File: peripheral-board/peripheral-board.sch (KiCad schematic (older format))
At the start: 1 part

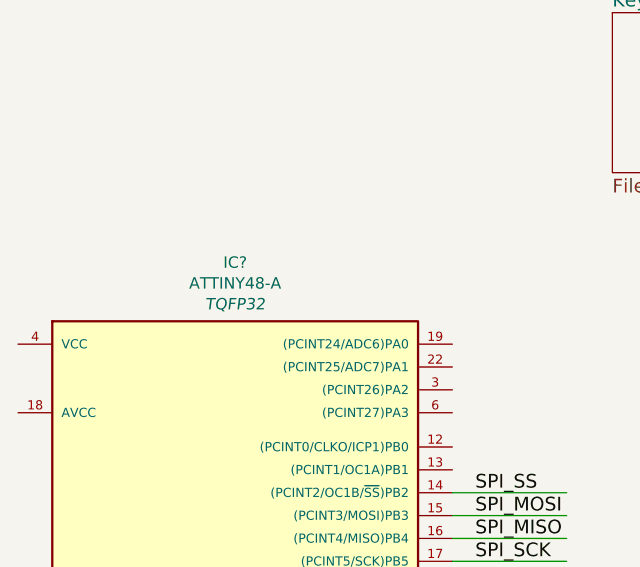
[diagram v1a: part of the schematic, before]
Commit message: added button 3d model
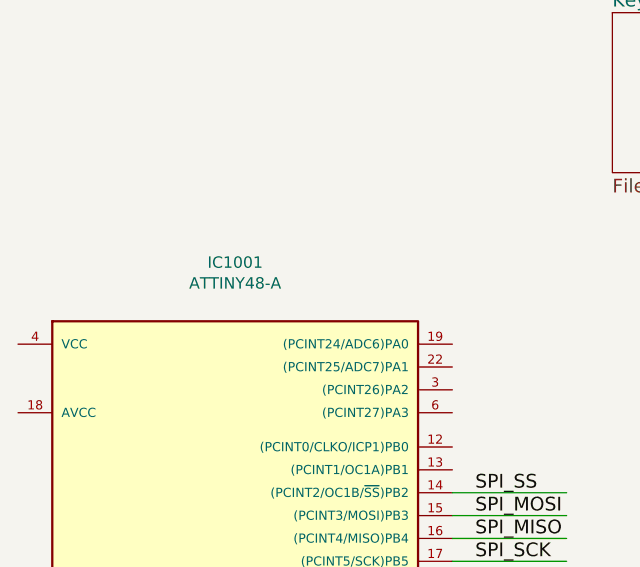
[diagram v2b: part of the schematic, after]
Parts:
- IC1001: renamed from IC?; footprint TQFP32 -> Housings_QFP:TQFP-32_7x7mm_Pitch0.8mm
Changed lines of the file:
@@
 $EndSheet
 $Comp
-L ATTINY48-A IC?
+L ATTINY48-A IC1001
 U 1 1 5819EBDE
 P 2950 4200
-F 0 "IC?" H 2950 5957 50  0000 C CNN
+F 0 "IC1001" H 2950 5957 50  0000 C CNN
 F 1 "ATTINY48-A" H 2950 5866 50  0000 C CNN
-F 2 "TQFP32" H 2950 5775 50  0000 C CIN
+F 2 "Housings_QFP:TQFP-32_7x7mm_Pitch0.8mm" H 2950 5775 50  0001 C CIN
 F 3 "" H 2950 4200 50  0000 C CNN
 	1    2950 4200

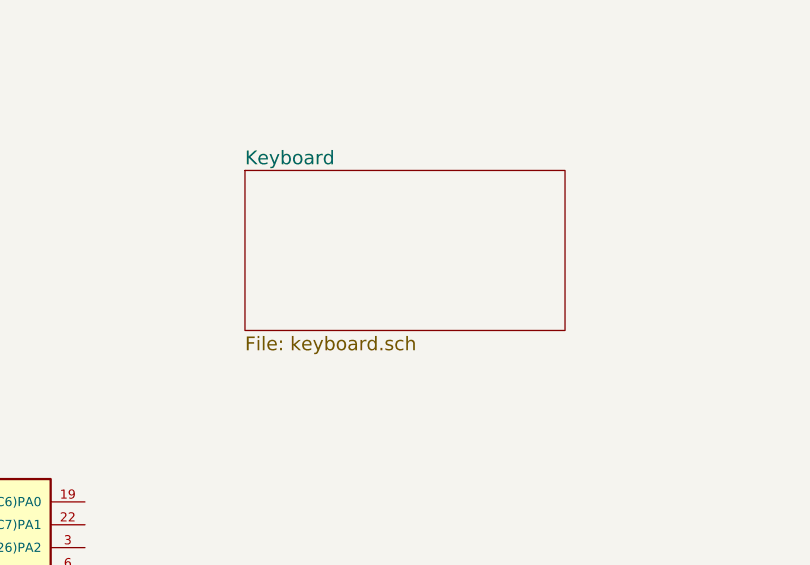
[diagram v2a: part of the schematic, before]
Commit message: added keyboard scanning logic
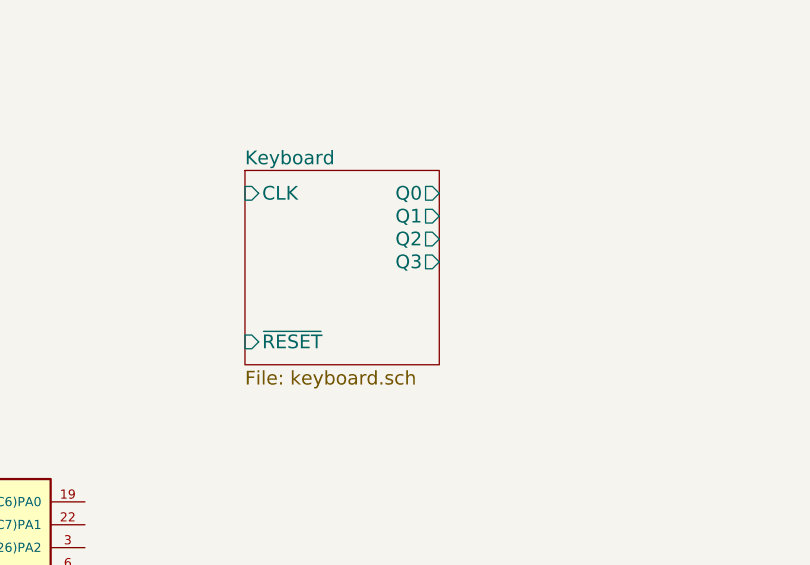
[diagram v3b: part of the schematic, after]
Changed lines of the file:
@@
 $EndDescr
 $Sheet
-S 4600 1350 1400 700
+S 4600 1350 850  850
 U 581919F6
 F0 "Keyboard" 60
 F1 "keyboard.sch" 60
+F2 "Q0" O R 5450 1450 60
+F3 "Q1" O R 5450 1550 60
+F4 "Q2" O R 5450 1650 60
+F5 "Q3" O R 5450 1750 60
+F6 "CLK" I L 4600 1450 60
+F7 "~RESET" I L 4600 2100 60
 $EndSheet
 $Sheet

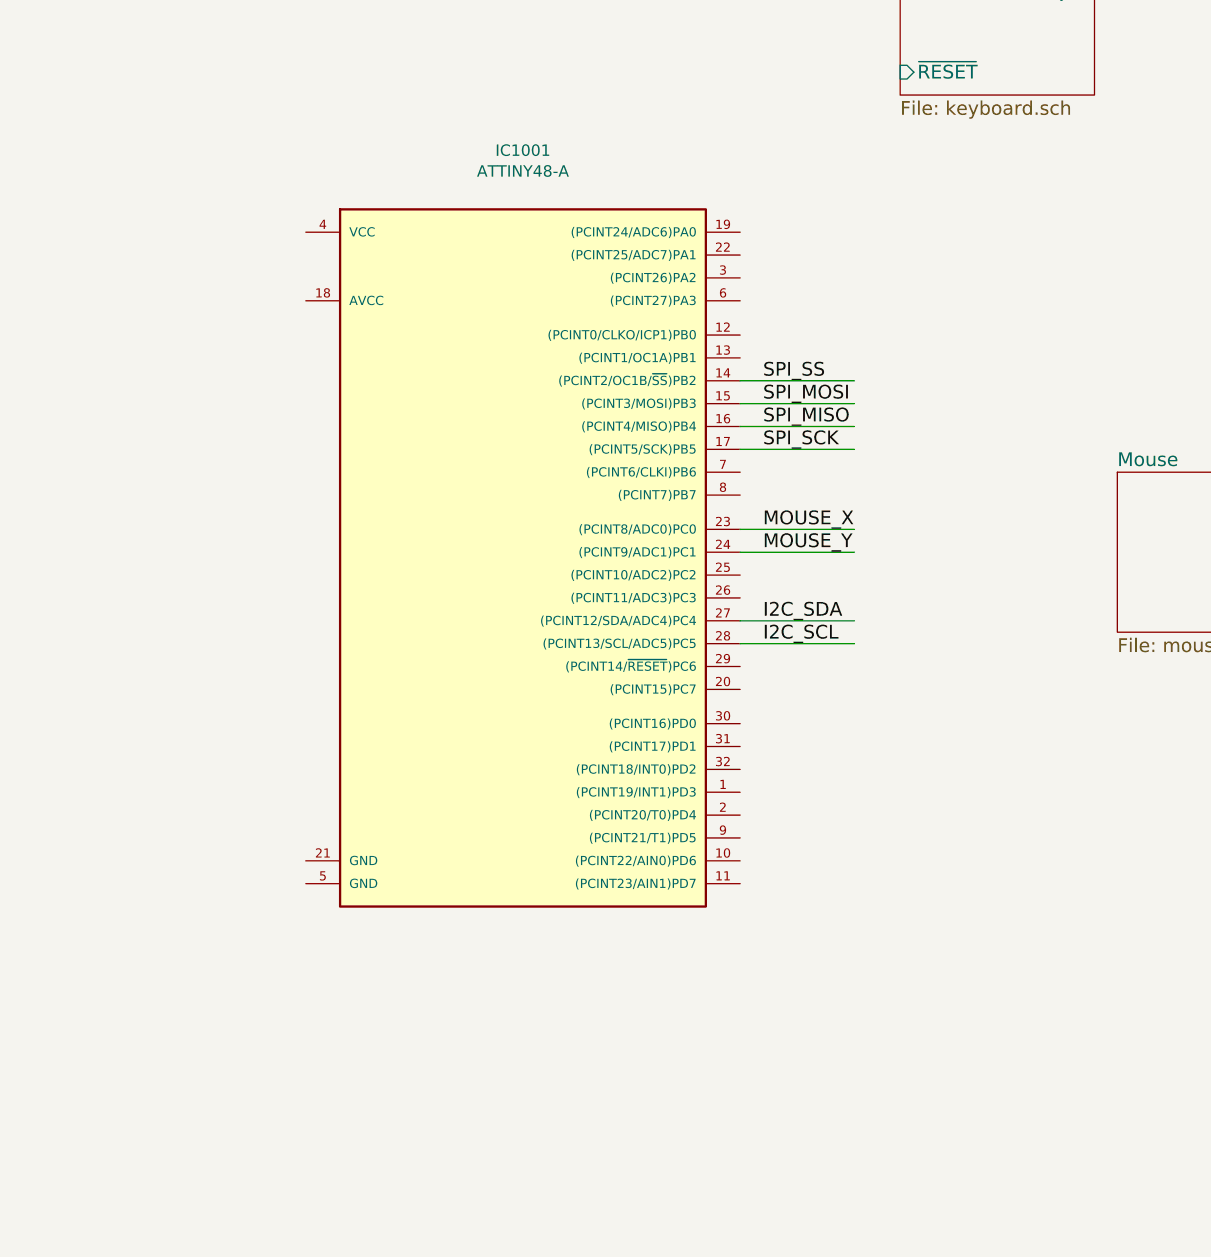
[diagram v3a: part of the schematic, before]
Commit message: added peripheral board bus header
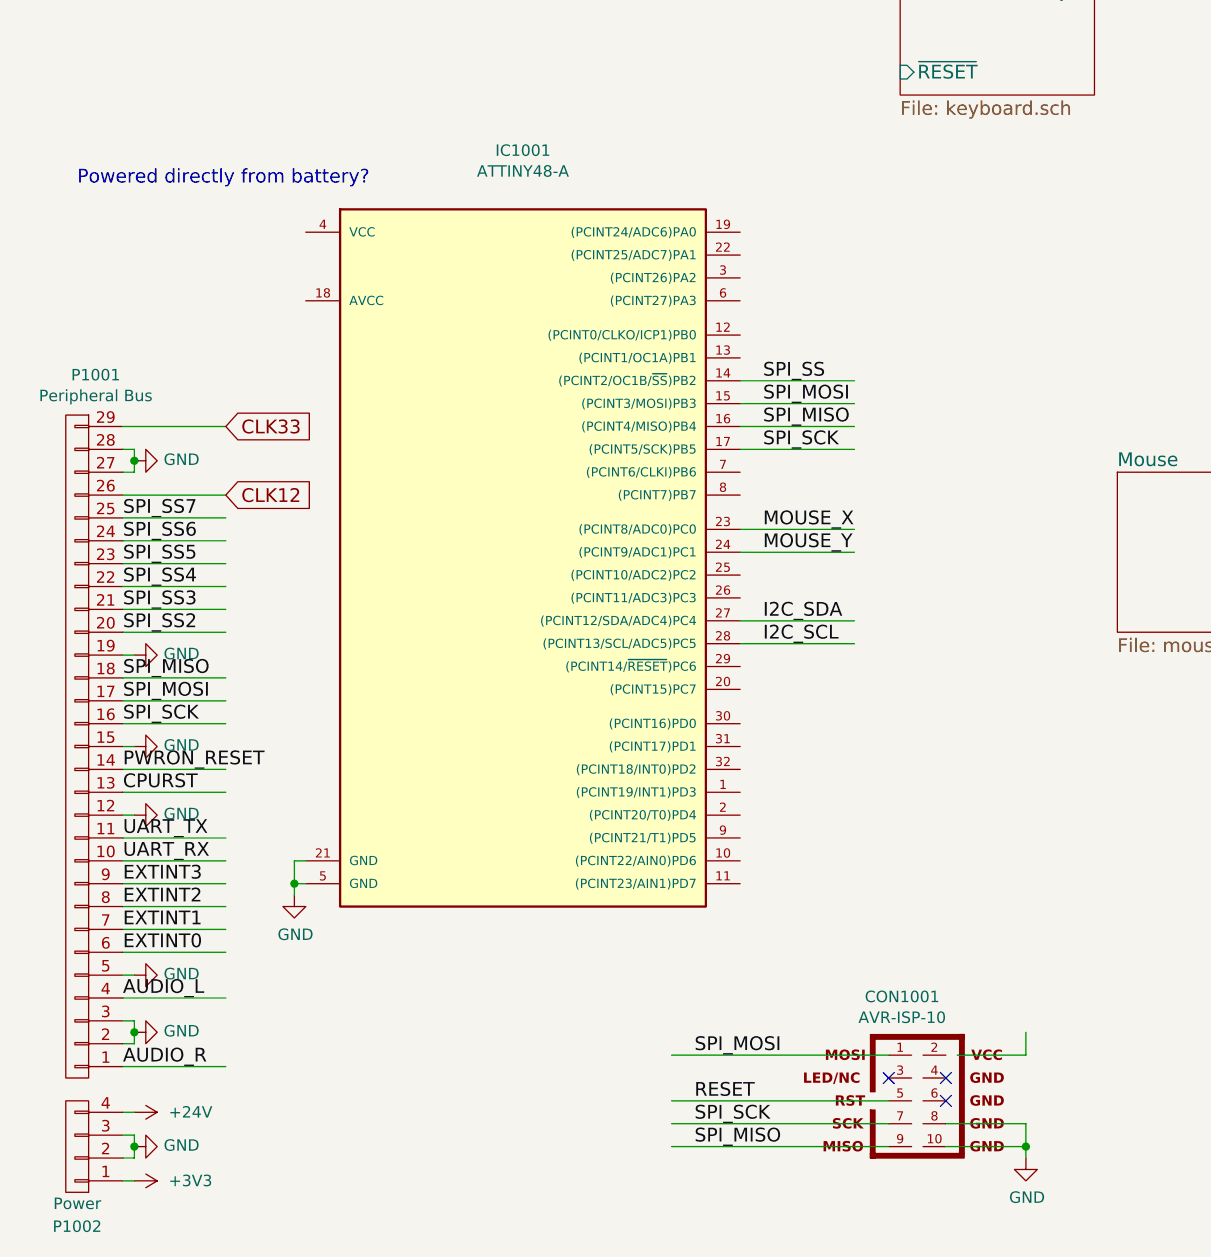
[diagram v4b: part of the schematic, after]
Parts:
- added CON1001: AVR-ISP-10, Connect:IDC_Header_Straight_10pins, symbol AVR-ISP-10
- added P1001: Peripheral Bus, Socket_Strips:Socket_Strip_Straight_1x29, symbol CONN_01X29
- added P1002: Power, Socket_Strips:Socket_Strip_Straight_1x04, symbol CONN_01X04
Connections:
- net labels added: +24V, +3V3, AUDIO_L, AUDIO_R, CLK12, CLK33, CPURST, EXTINT0, EXTINT1, EXTINT2, EXTINT3, GND, PWRON_RESET, RESET, SPI_SS2, SPI_SS3, SPI_SS4, SPI_SS5, SPI_SS6, SPI_SS7, UART_RX, UART_TX
- wire segments 8 -> 56
- no-connect marks 0 -> 3
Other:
- note added: "Powered directly from battery?"
